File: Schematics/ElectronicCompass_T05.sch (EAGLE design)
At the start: 64 parts, among them Q1 FDN360P, Q2 FDN360P, Q3 FDN360P, Q4 FDN360P, U1 ATMEGA32U4, X1 USBSMD, Y1 16MHz

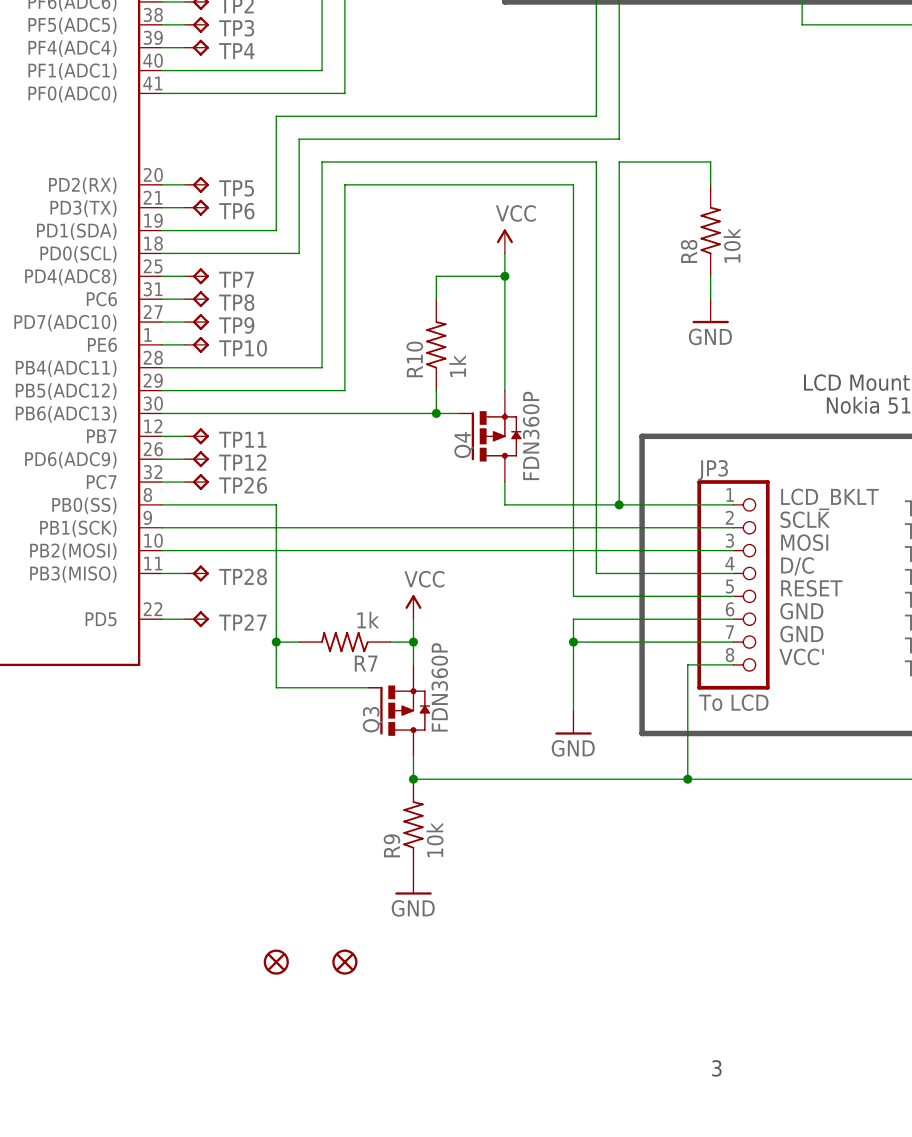
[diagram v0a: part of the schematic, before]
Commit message: Fixed transistor switches
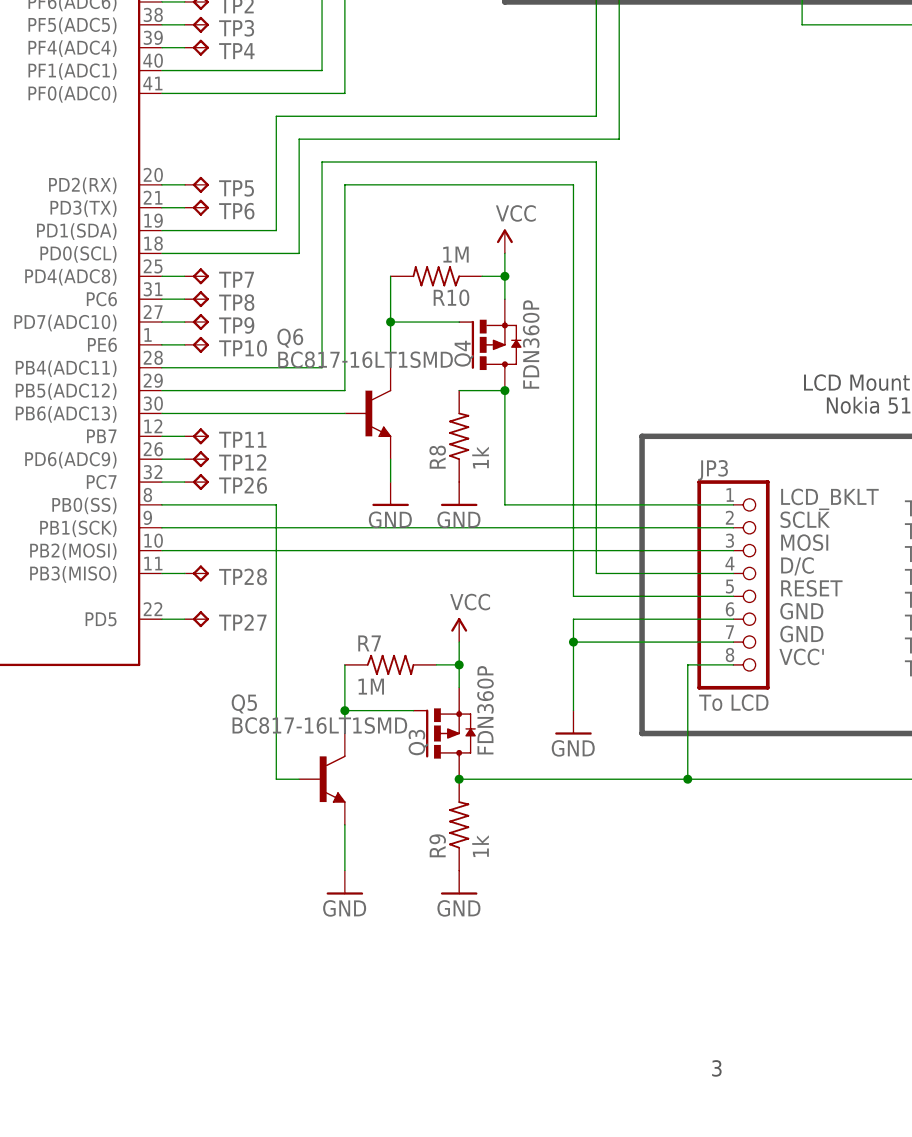
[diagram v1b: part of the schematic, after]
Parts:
- removed JP6, JP7: FIDUCIALUFIDUCIAL, SparkFun:FIDUCIALUFIDUCIAL
- added Q5, Q6: BC817-16LT1SMD, transistor-npn:BC817-16LT1SMD
- R10, R7: value 1k -> 1M
- R8, R9: value 10k -> 1k
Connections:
- new net N$44: Q6.B, U1.PB6(ADC13)
- new net N$45: Q3.G, Q5.C, R7.1
- net GND: now also Q5.E, Q6.E
- net N$26: now also Q6.C, R10.2; no longer R10.1, U1.PB6(ADC13)
- net N$37: now also Q5.B; no longer Q3.G, R7.2
- net VCC: now also R10.1, R7.2; no longer R10.2, R7.1
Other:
- moved on the sheet: Q3, Q4, R10, R7, R8, R9

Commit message: sch changes
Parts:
- removed S2: ON/OFF, switch-dil:DS01E
- added JP5: ON/OFF, pinhead:PINHD-1X2
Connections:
- removed net N$11: C7.2, U1.AVCC@24, U1.AVCC@44, U1.VCC@14, U1.VCC@34
- net GND: now also C7.2
- net N$36: now also JP5.1; no longer S2.1
- net VCC: now also JP5.2, U1.AVCC@24, U1.AVCC@44, U1.VCC@14, U1.VCC@34; no longer S2.2
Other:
- moved on the sheet: C10, C7, TP24
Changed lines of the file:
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@@
 <part name="TP22" library="testpad" deviceset="TP" device="TP06R"/>
 <part name="TP23" library="testpad" deviceset="TP" device="TP06R"/>
-<part name="S2" library="switch-dil" deviceset="DS01E" device="" value="ON/OFF"/>
 <part name="TP24" library="testpad" deviceset="TP" device="TP06R"/>
 <part name="TP25" library="testpad" deviceset="TP" device="TP06R"/>
@@
 <part name="GND20" library="supply1" deviceset="GND" device=""/>
 <part name="GND21" library="supply1" deviceset="GND" device=""/>
+<part name="JP5" library="pinhead" deviceset="PINHD-1X2" device="" value="ON/OFF"/>
+<part name="GND22" library="SparkFun" deviceset="GND" device=""/>
 </parts>
 <sheets>
@@
 </instance>
 <instance part="S1" gate="G$1" x="106.68" y="22.86"/>
-<instance part="GND1" gate="1" x="99.06" y="15.24"/>
+<instance part="GND1" gate="1" x="93.98" y="15.24"/>
 <instance part="P+1" gate="1" x="116.84" y="45.72" smashed="yes">
 <attribute name="VALUE" x="115.824" y="49.276" size="1.778" layer="96"/>
@@
 </instance>
 <instance part="C5" gate="G$1" x="30.48" y="43.18"/>
-<instance part="C10" gate="G$1" x="91.44" y="63.5"/>
+<instance part="C10" gate="G$1" x="88.9" y="63.5"/>
 <instance part="C11" gate="G$1" x="5.08" y="43.18"/>
-<instance part="GND5" gate="1" x="91.44" y="5.08" smashed="yes">
-<attribute name="VALUE" x="88.9" y="2.54" size="1.778" layer="96"/>
+<instance part="GND5" gate="1" x="88.9" y="5.08" smashed="yes">
+<attribute name="VALUE" x="86.36" y="2.54" size="1.778" layer="96"/>
 </instance>
 <instance part="GND9" gate="1" x="50.8" y="5.08"/>
@@
 <attribute name="TP_SIGNAL_NAME" x="252.73" y="-52.07" size="1.778" layer="97" rot="R90"/>
 </instance>
-<instance part="S2" gate="1" x="104.14" y="68.58" rot="R270"/>
-<instance part="TP24" gate="G$1" x="83.82" y="38.1" smashed="yes" rot="R270">
-<attribute name="NAME" x="85.09" y="36.83" size="1.778" layer="95"/>
-<attribute name="TP_SIGNAL_NAME" x="82.55" y="36.83" size="1.778" layer="97" rot="R270"/>
+<instance part="TP24" gate="G$1" x="81.28" y="38.1" smashed="yes" rot="R270">
+<attribute name="NAME" x="82.55" y="36.83" size="1.778" layer="95"/>
+<attribute name="TP_SIGNAL_NAME" x="80.01" y="36.83" size="1.778" layer="97" rot="R270"/>
 </instance>
 <instance part="TP25" gate="G$1" x="78.74" y="73.66"/>
@@
 <instance part="GND3" gate="1" x="96.52" y="-30.48"/>
 <instance part="GND6" gate="1" x="22.86" y="5.08"/>
-<instance part="C7" gate="G$1" x="124.46" y="38.1"/>
+<instance part="C7" gate="G$1" x="96.52" y="7.62"/>
 <instance part="R7" gate="G$1" x="187.96" y="-53.34" smashed="yes">
 <attribute name="NAME" x="184.15" y="-51.8414" size="1.778" layer="95"/>
@@
 <instance part="GND20" gate="1" x="182.88" y="-78.74"/>
 <instance part="GND21" gate="1" x="187.96" y="-35.56"/>
+<instance part="JP5" gate="G$1" x="104.14" y="71.12" smashed="yes" rot="R90">
+<attribute name="NAME" x="105.41" y="75.565" size="1.778" layer="95" rot="R180"/>
+<attribute name="VALUE" x="107.95" y="63.5" size="1.778" layer="96" rot="R180"/>
+</instance>
+<instance part="GND22" gate="1" x="96.52" y="0"/>
 </instances>
 <busses>
@@
 <net name="GND" class="0">
 <segment>
-<wire x1="99.06" y1="17.78" x2="99.06" y2="22.86" width="0.1524" layer="91"/>
-<wire x1="99.06" y1="22.86" x2="101.6" y2="22.86" width="0.1524" layer="91"/>
+<wire x1="93.98" y1="17.78" x2="93.98" y2="22.86" width="0.1524" layer="91"/>
+<wire x1="93.98" y1="22.86" x2="101.6" y2="22.86" width="0.1524" layer="91"/>
 <pinref part="GND1" gate="1" pin="GND"/>
 <pinref part="S1" gate="G$1" pin="1"/>
@@
 <pinref part="C10" gate="G$1" pin="2"/>
 <pinref part="GND5" gate="1" pin="GND"/>
-<wire x1="91.44" y1="7.62" x2="91.44" y2="58.42" width="0.1524" layer="91"/>
+<wire x1="88.9" y1="7.62" x2="88.9" y2="58.42" width="0.1524" layer="91"/>
 </segment>
 <segment>
@@
 <wire x1="187.96" y1="-30.48" x2="187.96" y2="-33.02" width="0.1524" layer="91"/>
 </segment>
+<segment>
+<pinref part="C7" gate="G$1" pin="2"/>
+<pinref part="GND22" gate="1" pin="GND"/>
+</segment>
 </net>
 <net name="VCC" class="0">
@@
 <pinref part="P+3" gate="VCC" pin="VCC"/>
 <wire x1="116.84" y1="73.66" x2="116.84" y2="68.58" width="0.1524" layer="91"/>
-<pinref part="S2" gate="1" pin="2"/>
-<wire x1="116.84" y1="68.58" x2="109.22" y2="68.58" width="0.1524" layer="91"/>
+<wire x1="116.84" y1="68.58" x2="104.14" y2="68.58" width="0.1524" layer="91"/>
+<pinref part="JP5" gate="G$1" pin="2"/>
 </segment>
 <segment>
@@
 </segment>
 <segment>
-<pinref part="P+2" gate="1" pin="VCC"/>
-<pinref part="C7" gate="G$1" pin="1"/>
-<wire x1="124.46" y1="45.72" x2="124.46" y2="40.64" width="0.1524" layer="91"/>
-</segment>
-<segment>
 <pinref part="P+6" gate="1" pin="VCC"/>
 <pinref part="Q3" gate="G$1" pin="S"/>
@@
 <wire x1="193.04" y1="-53.34" x2="195.58" y2="-53.34" width="0.1524" layer="91"/>
 <junction x="195.58" y="-53.34"/>
+</segment>
+<segment>
+<wire x1="127" y1="20.32" x2="124.46" y2="20.32" width="0.1524" layer="91"/>
+<wire x1="127" y1="17.78" x2="124.46" y2="17.78" width="0.1524" layer="91"/>
+<wire x1="124.46" y1="17.78" x2="124.46" y2="20.32" width="0.1524" layer="91"/>
+<wire x1="127" y1="15.24" x2="124.46" y2="15.24" width="0.1524" layer="91"/>
+<wire x1="124.46" y1="15.24" x2="124.46" y2="17.78" width="0.1524" layer="91"/>
+<wire x1="127" y1="12.7" x2="124.46" y2="12.7" width="0.1524" layer="91"/>
+<wire x1="124.46" y1="12.7" x2="124.46" y2="15.24" width="0.1524" layer="91"/>
+<junction x="124.46" y="17.78"/>
+<junction x="124.46" y="15.24"/>
+<pinref part="U1" gate="G$1" pin="VCC@14"/>
+<pinref part="U1" gate="G$1" pin="VCC@34"/>
+<pinref part="U1" gate="G$1" pin="AVCC@24"/>
+<pinref part="U1" gate="G$1" pin="AVCC@44"/>
+<pinref part="P+2" gate="1" pin="VCC"/>
+<wire x1="124.46" y1="45.72" x2="124.46" y2="17.78" width="0.1524" layer="91"/>
+<pinref part="C7" gate="G$1" pin="1"/>
+<wire x1="124.46" y1="15.24" x2="96.52" y2="15.24" width="0.1524" layer="91"/>
+<wire x1="96.52" y1="15.24" x2="96.52" y2="10.16" width="0.1524" layer="91"/>
 </segment>
 </net>
@@
 <wire x1="68.58" y1="38.1" x2="78.74" y2="38.1" width="0.1524" layer="91"/>
 <pinref part="TP24" gate="G$1" pin="TP"/>
-<wire x1="78.74" y1="38.1" x2="81.28" y2="38.1" width="0.1524" layer="91"/>
 <pinref part="Q2" gate="G$1" pin="D"/>
 <wire x1="78.74" y1="38.1" x2="78.74" y2="45.72" width="0.1524" layer="91"/>
@@
 <wire x1="68.58" y1="68.58" x2="78.74" y2="68.58" width="0.1524" layer="91"/>
 <junction x="78.74" y="68.58"/>
-<pinref part="S2" gate="1" pin="1"/>
-<wire x1="99.06" y1="68.58" x2="91.44" y2="68.58" width="0.1524" layer="91"/>
+<wire x1="101.6" y1="68.58" x2="88.9" y2="68.58" width="0.1524" layer="91"/>
 <pinref part="C10" gate="G$1" pin="1"/>
-<wire x1="91.44" y1="68.58" x2="78.74" y2="68.58" width="0.1524" layer="91"/>
-<wire x1="91.44" y1="66.04" x2="91.44" y2="68.58" width="0.1524" layer="91"/>
-<junction x="91.44" y="68.58"/>
+<wire x1="88.9" y1="68.58" x2="78.74" y2="68.58" width="0.1524" layer="91"/>
+<wire x1="88.9" y1="66.04" x2="88.9" y2="68.58" width="0.1524" layer="91"/>
+<junction x="88.9" y="68.58"/>
 <pinref part="U$1" gate="G$1" pin="OUT"/>
+<pinref part="JP5" gate="G$1" pin="1"/>
 </segment>
 </net>
@@
 </segment>
 </net>
-<net name="N$11" class="0">
-<segment>
-<wire x1="127" y1="20.32" x2="124.46" y2="20.32" width="0.1524" layer="91"/>
-<wire x1="127" y1="17.78" x2="124.46" y2="17.78" width="0.1524" layer="91"/>
-<wire x1="124.46" y1="17.78" x2="124.46" y2="20.32" width="0.1524" layer="91"/>
-<wire x1="127" y1="15.24" x2="124.46" y2="15.24" width="0.1524" layer="91"/>
-<wire x1="124.46" y1="15.24" x2="124.46" y2="17.78" width="0.1524" layer="91"/>
-<wire x1="127" y1="12.7" x2="124.46" y2="12.7" width="0.1524" layer="91"/>
-<wire x1="124.46" y1="12.7" x2="124.46" y2="15.24" width="0.1524" layer="91"/>
-<junction x="124.46" y="17.78"/>
-<junction x="124.46" y="15.24"/>
-<pinref part="U1" gate="G$1" pin="VCC@14"/>
-<pinref part="U1" gate="G$1" pin="VCC@34"/>
-<pinref part="U1" gate="G$1" pin="AVCC@24"/>
-<pinref part="U1" gate="G$1" pin="AVCC@44"/>
-<pinref part="C7" gate="G$1" pin="2"/>
-<wire x1="124.46" y1="33.02" x2="124.46" y2="20.32" width="0.1524" layer="91"/>
-<junction x="124.46" y="20.32"/>
-</segment>
-</net>

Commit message: New components
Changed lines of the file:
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@@
 <pinref part="U1" gate="G$1" pin="AVCC@44"/>
 <pinref part="P+2" gate="1" pin="VCC"/>
-<wire x1="124.46" y1="45.72" x2="124.46" y2="17.78" width="0.1524" layer="91"/>
+<wire x1="124.46" y1="45.72" x2="124.46" y2="20.32" width="0.1524" layer="91"/>
 <pinref part="C7" gate="G$1" pin="1"/>
+<wire x1="124.46" y1="20.32" x2="124.46" y2="17.78" width="0.1524" layer="91"/>
 <wire x1="124.46" y1="15.24" x2="96.52" y2="15.24" width="0.1524" layer="91"/>
 <wire x1="96.52" y1="15.24" x2="96.52" y2="10.16" width="0.1524" layer="91"/>
+<junction x="124.46" y="20.32"/>
 </segment>
 </net>

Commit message: sch changes
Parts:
- added C8: 1uF, rcl:C-USC0805
- added R11: 10k, resistor:R-US_M0805
- added S2: Switch, switch-dil:DS01E
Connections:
- new net N$11: C8.1, R11.1, S2.2, U1.PE2/!HWB
- net GND: now also C8.2, S2.1; no longer U1.PE2/!HWB
- net VCC: now also R11.2
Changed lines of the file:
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@@
 <part name="JP5" library="pinhead" deviceset="PINHD-1X2" device="" value="ON/OFF"/>
 <part name="GND22" library="SparkFun" deviceset="GND" device=""/>
+<part name="GND23" library="SparkFun" deviceset="GND" device=""/>
+<part name="P+5" library="supply1" deviceset="VCC" device=""/>
+<part name="S2" library="switch-dil" deviceset="DS01E" device="" value="Switch"/>
+<part name="C8" library="rcl" deviceset="C-US" device="C0805" value="1uF"/>
+<part name="GND24" library="SparkFun" deviceset="GND" device=""/>
+<part name="R11" library="resistor" deviceset="R-US_" device="M0805" value="10k"/>
 </parts>
 <sheets>
@@
 </instance>
 <instance part="GND4" gate="1" x="0" y="-30.48"/>
-<instance part="GND7" gate="1" x="104.14" y="-55.88"/>
+<instance part="GND7" gate="1" x="114.3" y="-55.88"/>
 <instance part="R4" gate="G$1" x="30.48" y="15.24" rot="R90"/>
 <instance part="R5" gate="G$1" x="27.94" y="55.88"/>
@@
 </instance>
 <instance part="GND22" gate="1" x="96.52" y="0"/>
+<instance part="GND23" gate="1" x="81.28" y="-68.58"/>
+<instance part="P+5" gate="VCC" x="99.06" y="-38.1" smashed="yes">
+<attribute name="VALUE" x="101.6" y="-35.56" size="1.778" layer="96" rot="R180"/>
+</instance>
+<instance part="S2" gate="1" x="86.36" y="-58.42" rot="R270"/>
+<instance part="C8" gate="G$1" x="99.06" y="-60.96"/>
+<instance part="GND24" gate="1" x="99.06" y="-68.58"/>
+<instance part="R11" gate="G$1" x="99.06" y="-48.26" smashed="yes" rot="R90">
+<attribute name="NAME" x="97.5614" y="-52.07" size="1.778" layer="95" rot="R90"/>
+<attribute name="VALUE" x="102.362" y="-52.07" size="1.778" layer="96" rot="R90"/>
+</instance>
 </instances>
 <busses>
@@
 </segment>
 <segment>
-<wire x1="104.14" y1="-53.34" x2="104.14" y2="-50.8" width="0.1524" layer="91"/>
-<wire x1="104.14" y1="-50.8" x2="127" y2="-50.8" width="0.1524" layer="91"/>
-<wire x1="104.14" y1="-50.8" x2="104.14" y2="-48.26" width="0.1524" layer="91"/>
-<wire x1="104.14" y1="-48.26" x2="127" y2="-48.26" width="0.1524" layer="91"/>
-<wire x1="104.14" y1="-48.26" x2="104.14" y2="-45.72" width="0.1524" layer="91"/>
-<wire x1="104.14" y1="-45.72" x2="127" y2="-45.72" width="0.1524" layer="91"/>
-<wire x1="104.14" y1="-45.72" x2="104.14" y2="-43.18" width="0.1524" layer="91"/>
-<wire x1="104.14" y1="-43.18" x2="127" y2="-43.18" width="0.1524" layer="91"/>
-<wire x1="104.14" y1="-43.18" x2="104.14" y2="-40.64" width="0.1524" layer="91"/>
-<wire x1="104.14" y1="-40.64" x2="127" y2="-40.64" width="0.1524" layer="91"/>
-<wire x1="104.14" y1="-40.64" x2="104.14" y2="-33.02" width="0.1524" layer="91"/>
-<wire x1="104.14" y1="-33.02" x2="127" y2="-33.02" width="0.1524" layer="91"/>
-<junction x="104.14" y="-50.8"/>
-<junction x="104.14" y="-48.26"/>
-<junction x="104.14" y="-45.72"/>
-<junction x="104.14" y="-43.18"/>
-<junction x="104.14" y="-40.64"/>
+<wire x1="114.3" y1="-53.34" x2="114.3" y2="-50.8" width="0.1524" layer="91"/>
+<wire x1="114.3" y1="-50.8" x2="127" y2="-50.8" width="0.1524" layer="91"/>
+<wire x1="114.3" y1="-50.8" x2="114.3" y2="-48.26" width="0.1524" layer="91"/>
+<wire x1="114.3" y1="-48.26" x2="127" y2="-48.26" width="0.1524" layer="91"/>
+<wire x1="114.3" y1="-48.26" x2="114.3" y2="-45.72" width="0.1524" layer="91"/>
+<wire x1="114.3" y1="-45.72" x2="127" y2="-45.72" width="0.1524" layer="91"/>
+<wire x1="114.3" y1="-45.72" x2="114.3" y2="-43.18" width="0.1524" layer="91"/>
+<wire x1="114.3" y1="-43.18" x2="127" y2="-43.18" width="0.1524" layer="91"/>
+<wire x1="114.3" y1="-43.18" x2="114.3" y2="-40.64" width="0.1524" layer="91"/>
+<wire x1="114.3" y1="-40.64" x2="127" y2="-40.64" width="0.1524" layer="91"/>
+<junction x="114.3" y="-50.8"/>
+<junction x="114.3" y="-48.26"/>
+<junction x="114.3" y="-45.72"/>
+<junction x="114.3" y="-43.18"/>
 <pinref part="GND7" gate="1" pin="GND"/>
 <pinref part="U1" gate="G$1" pin="GND@43"/>
@@
 <pinref part="U1" gate="G$1" pin="GND@15"/>
 <pinref part="U1" gate="G$1" pin="UGND"/>
-<pinref part="U1" gate="G$1" pin="PE2/!HWB"/>
 </segment>
 <segment>
@@
 <pinref part="C7" gate="G$1" pin="2"/>
 <pinref part="GND22" gate="1" pin="GND"/>
+</segment>
+<segment>
+<wire x1="81.28" y1="-58.42" x2="81.28" y2="-66.04" width="0.1524" layer="91"/>
+<pinref part="GND23" gate="1" pin="GND"/>
+<pinref part="S2" gate="1" pin="1"/>
+</segment>
+<segment>
+<pinref part="C8" gate="G$1" pin="2"/>
+<pinref part="GND24" gate="1" pin="GND"/>
 </segment>
 </net>
@@
 <wire x1="96.52" y1="15.24" x2="96.52" y2="10.16" width="0.1524" layer="91"/>
 <junction x="124.46" y="20.32"/>
+</segment>
+<segment>
+<pinref part="P+5" gate="VCC" pin="VCC"/>
+<wire x1="99.06" y1="-40.64" x2="99.06" y2="-43.18" width="0.1524" layer="91"/>
+<pinref part="R11" gate="G$1" pin="2"/>
 </segment>
 </net>
@@
 </segment>
 </net>
+<net name="N$11" class="0">
+<segment>
+<pinref part="U1" gate="G$1" pin="PE2/!HWB"/>
+<wire x1="106.68" y1="-33.02" x2="127" y2="-33.02" width="0.1524" layer="91"/>
+<wire x1="106.68" y1="-33.02" x2="106.68" y2="-58.42" width="0.1524" layer="91"/>
+<wire x1="106.68" y1="-58.42" x2="99.06" y2="-58.42" width="0.1524" layer="91"/>
+<pinref part="S2" gate="1" pin="2"/>
+<junction x="99.06" y="-58.42"/>
+<pinref part="C8" gate="G$1" pin="1"/>
+<wire x1="99.06" y1="-53.34" x2="99.06" y2="-58.42" width="0.1524" layer="91"/>
+<wire x1="99.06" y1="-58.42" x2="91.44" y2="-58.42" width="0.1524" layer="91"/>
+<pinref part="R11" gate="G$1" pin="1"/>
+</segment>
+</net>

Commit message: sch update
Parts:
- removed JP5: ON/OFF, pinhead:PINHD-1X2
- added S3: Off/On, switch-dil:DS01E
- S2: value Switch -> Pgm/Run
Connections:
- net N$36: now also S3.1; no longer JP5.1
- net VCC: now also S3.2; no longer JP5.2
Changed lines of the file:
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@@
 <part name="GND20" library="supply1" deviceset="GND" device=""/>
 <part name="GND21" library="supply1" deviceset="GND" device=""/>
-<part name="JP5" library="pinhead" deviceset="PINHD-1X2" device="" value="ON/OFF"/>
 <part name="GND22" library="SparkFun" deviceset="GND" device=""/>
 <part name="GND23" library="SparkFun" deviceset="GND" device=""/>
 <part name="P+5" library="supply1" deviceset="VCC" device=""/>
-<part name="S2" library="switch-dil" deviceset="DS01E" device="" value="Switch"/>
+<part name="S2" library="switch-dil" deviceset="DS01E" device="" value="Pgm/Run"/>
 <part name="C8" library="rcl" deviceset="C-US" device="C0805" value="1uF"/>
 <part name="GND24" library="SparkFun" deviceset="GND" device=""/>
 <part name="R11" library="resistor" deviceset="R-US_" device="M0805" value="10k"/>
+<part name="S3" library="switch-dil" deviceset="DS01E" device="" value="Off/On"/>
 </parts>
 <sheets>
@@
 <instance part="GND20" gate="1" x="182.88" y="-78.74"/>
 <instance part="GND21" gate="1" x="187.96" y="-35.56"/>
-<instance part="JP5" gate="G$1" x="104.14" y="71.12" smashed="yes" rot="R90">
-<attribute name="NAME" x="105.41" y="75.565" size="1.778" layer="95" rot="R180"/>
-<attribute name="VALUE" x="107.95" y="63.5" size="1.778" layer="96" rot="R180"/>
-</instance>
 <instance part="GND22" gate="1" x="96.52" y="0"/>
 <instance part="GND23" gate="1" x="81.28" y="-68.58"/>
@@
 <attribute name="VALUE" x="102.362" y="-52.07" size="1.778" layer="96" rot="R90"/>
 </instance>
+<instance part="S3" gate="1" x="104.14" y="68.58" rot="R270"/>
 </instances>
 <busses>
@@
 <pinref part="P+3" gate="VCC" pin="VCC"/>
 <wire x1="116.84" y1="73.66" x2="116.84" y2="68.58" width="0.1524" layer="91"/>
-<wire x1="116.84" y1="68.58" x2="104.14" y2="68.58" width="0.1524" layer="91"/>
-<pinref part="JP5" gate="G$1" pin="2"/>
+<wire x1="116.84" y1="68.58" x2="109.22" y2="68.58" width="0.1524" layer="91"/>
+<pinref part="S3" gate="1" pin="2"/>
 </segment>
 <segment>
@@
 <wire x1="68.58" y1="68.58" x2="78.74" y2="68.58" width="0.1524" layer="91"/>
 <junction x="78.74" y="68.58"/>
-<wire x1="101.6" y1="68.58" x2="88.9" y2="68.58" width="0.1524" layer="91"/>
 <pinref part="C10" gate="G$1" pin="1"/>
 <wire x1="88.9" y1="68.58" x2="78.74" y2="68.58" width="0.1524" layer="91"/>
 <wire x1="88.9" y1="66.04" x2="88.9" y2="68.58" width="0.1524" layer="91"/>
-<junction x="88.9" y="68.58"/>
 <pinref part="U$1" gate="G$1" pin="OUT"/>
-<pinref part="JP5" gate="G$1" pin="1"/>
-</segment>
-</net>
+<pinref part="S3" gate="1" pin="1"/>
+<wire x1="88.9" y1="68.58" x2="99.06" y2="68.58" width="0.1524" layer="91"/>
+</segment>
+</net>
